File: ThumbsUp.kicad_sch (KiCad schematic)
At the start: 42 parts, among them J10 Raiser_Male, J13 Raiser_Female, J14 Raiser_Male, J19 Raiser_Female, J1L1 PJ-3200B, J1R1 PJ-3200B, J33 Raiser_Male, J34 Raiser_Female, J35 Raiser_Male, J38 Raiser_Female, J39 Raiser_Male, J40 Raiser_Female, J41 Raiser_Male, J47 Raiser_Female, J48 Raiser_Male, J9 Raiser_Female, U1 ProMicro

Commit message: K12: Modifying the layout, WIP.
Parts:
- added JP1: Handiness, Jumper:SolderJumper-2_P1.3mm_Open_RoundedPad1.0x1.5mm, symbol Jumper:SolderJumper_2_Open
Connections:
- net GND: now also JP1.1 (A)
- net at U1.7 (D4): now also JP1.2 (B)
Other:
- note added: "GP29 GP28 GP27 GP26 GP22 GP20 GP23 GP21"
- note added: "GP5 GP6 GP7 GP8 GP9"
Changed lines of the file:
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@@
 		)
 	)
+	(text "GP5\nGP6\nGP7\nGP8\nGP9"
+		(exclude_from_sim no)
+		(at 320.04 226.568 0)
+		(effects
+			(font
+				(size 1.27 1.27)
+			)
+		)
+	)
+	(text "GP29\nGP28\nGP27\nGP26\nGP22\nGP20\nGP23\nGP21"
+		(exclude_from_sim no)
+		(at 332.486 222.25 0)
+		(effects
+			(font
+				(size 1.27 1.27)
+			)
+		)
+	)
 	(junction
 		(at 303.53 308.61)
@@
 	(wire
 		(pts
+			(xy 295.91 218.44) (xy 297.18 218.44)
+		)
+		(stroke
+			(width 0)
+			(type default)
+		)
+	)
+	(wire
+		(pts
 			(xy 502.92 332.74) (xy 500.38 332.74)
 		)
@@
 	(wire
 		(pts
+			(xy 304.8 218.44) (xy 308.61 218.44)
+		)
+		(stroke
+			(width 0)
+			(type default)
+		)
+	)
+	(wire
+		(pts
 			(xy 438.15 199.39) (xy 438.15 207.01)
 		)
@@
 	(symbol
 		(lib_id "power:GND")
+		(at 295.91 218.44 0)
+		(unit 1)
+		(exclude_from_sim no)
+		(in_bom yes)
+		(on_board yes)
+		(dnp no)
+		(property "Reference" "#PWR08"
+			(at 295.91 224.79 0)
+			(effects
+				(font
+					(size 1.27 1.27)
+				)
+				(hide yes)
+			)
+		)
+		(property "Value" "GND"
+			(at 296.037 222.8342 0)
+			(effects
+				(font
+					(size 1.27 1.27)
+				)
+			)
+		)
+		(property "Footprint" ""
+			(at 295.91 218.44 0)
+			(effects
+				(font
+					(size 1.27 1.27)
+				)
+				(hide yes)
+			)
+		)
+		(property "Datasheet" ""
+			(at 295.91 218.44 0)
+			(effects
+				(font
+					(size 1.27 1.27)
+				)
+				(hide yes)
+			)
+		)
+		(property "Description" ""
+			(at 295.91 218.44 0)
+			(effects
+				(font
+					(size 1.27 1.27)
+				)
+			)
+		)
+		(pin "1"
+		)
+		(instances
+			(project "ThumbsUp"
+				(path "/467ed76c-995a-4514-a2e9-81ed0f98430e"
+					(reference "#PWR08")
+					(unit 1)
+				)
+			)
+		)
+	)
+	(symbol
+		(lib_id "power:GND")
 		(at 364.49 205.74 0)
 		(unit 1)
@@
 					(unit 1)
 				)
+			)
+		)
+	)
+	(symbol
+		(lib_id "Jumper:SolderJumper_2_Open")
+		(at 300.99 218.44 0)
+		(unit 1)
+		(exclude_from_sim no)
+		(in_bom no)
+		(on_board yes)
+		(dnp no)
+		(fields_autoplaced yes)
+		(property "Reference" "JP1"
+			(at 300.99 212.09 0)
+			(effects
+				(font
+					(size 1.27 1.27)
+				)
+			)
+		)
+		(property "Value" "Handiness"
+			(at 300.99 214.63 0)
+			(effects
+				(font
+					(size 1.27 1.27)
+				)
+			)
+		)
+		(property "Footprint" "Jumper:SolderJumper-2_P1.3mm_Open_RoundedPad1.0x1.5mm"
+			(at 300.99 218.44 0)
+			(effects
+				(font
+					(size 1.27 1.27)
+				)
+				(hide yes)
+			)
+		)
+		(property "Datasheet" "~"
+			(at 300.99 218.44 0)
+			(effects
+				(font
+					(size 1.27 1.27)
+				)
+				(hide yes)
+			)
+		)
+		(property "Description" "Solder Jumper, 2-pole, open"
+			(at 300.99 218.44 0)
+			(effects
+				(font
+					(size 1.27 1.27)
+				)
+				(hide yes)
+			)
+		)
+		(pin "1"
+		)
+		(pin "2"
+		)
+		(instances
+			(project ""
+				(path "/467ed76c-995a-4514-a2e9-81ed0f98430e"
+					(reference "JP1")
+					(unit 1)
+				)

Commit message: K12: Modifying the layout, WIP.
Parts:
- added H6: MountingHole_Pad, MountingHole:MountingHole_3.5mm_Pad, symbol Mechanical:MountingHole_Pad
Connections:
- net GNDB is gone; now on net GND: H3.1
- net GNDA: now also H6.1
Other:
- moved on the sheet: H1, H10, H15, H2

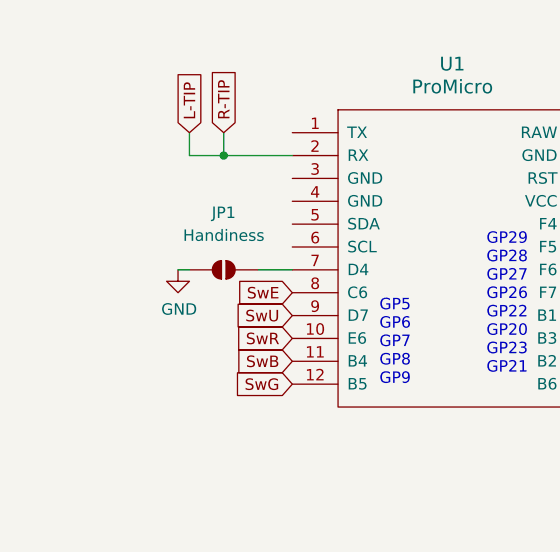
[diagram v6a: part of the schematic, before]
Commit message: K12: Added left-side handiness pull-up R, laid out all tracks. TODO: generate Gerbers.
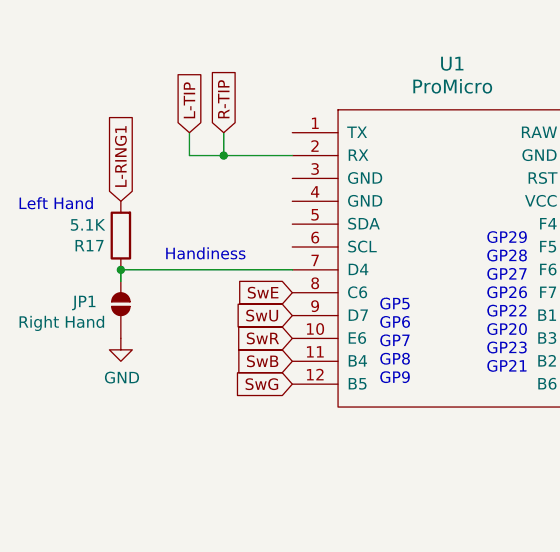
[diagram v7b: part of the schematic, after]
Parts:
- added R17: 5.1K, Resistor_SMD:R_0805_2012Metric, symbol Device:R
- JP1: value Handiness -> Right Hand
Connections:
- net +5V: now also R17.2
- net at JP1.2 (B), U1.7 (D4): now also R17.1
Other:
- note added: "Handiness"
- note added: "Left Hand"
- moved on the sheet: JP1
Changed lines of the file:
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@@
 		)
 	)
+	(text "Left Hand"
+		(exclude_from_sim no)
+		(at 278.13 212.09 0)
+		(effects
+			(font
+				(size 1.27 1.27)
+			)
+			(justify left bottom)
+		)
+	)
+	(text "Handiness"
+		(exclude_from_sim no)
+		(at 298.958 216.916 0)
+		(effects
+			(font
+				(size 1.27 1.27)
+			)
+		)
+	)
 	(junction
 		(at 303.53 308.61)
@@
 	)
 	(junction
+		(at 289.56 218.44)
+		(diameter 0)
+		(color 0 0 0 0)
+	)
+	(junction
 		(at 491.49 345.44)
 		(diameter 0)
@@
 	(wire
 		(pts
-			(xy 295.91 218.44) (xy 297.18 218.44)
+			(xy 502.92 332.74) (xy 500.38 332.74)
 		)
 		(stroke
@@
 	(wire
 		(pts
-			(xy 502.92 332.74) (xy 500.38 332.74)
+			(xy 414.02 345.44) (xy 416.56 345.44)
 		)
 		(stroke
@@
 	(wire
 		(pts
-			(xy 414.02 345.44) (xy 416.56 345.44)
+			(xy 317.5 299.72) (xy 328.93 299.72)
 		)
 		(stroke
@@
 	(wire
 		(pts
-			(xy 317.5 299.72) (xy 328.93 299.72)
+			(xy 289.56 219.71) (xy 289.56 218.44)
 		)
 		(stroke
@@
 	(wire
 		(pts
-			(xy 304.8 218.44) (xy 308.61 218.44)
-		)
-		(stroke
-			(width 0)
-			(type default)
-		)
-	)
-	(wire
-		(pts
 			(xy 438.15 199.39) (xy 438.15 207.01)
 		)
@@
 	(wire
 		(pts
+			(xy 289.56 218.44) (xy 308.61 218.44)
+		)
+		(stroke
+			(width 0)
+			(type default)
+		)
+	)
+	(wire
+		(pts
 			(xy 491.49 332.74) (xy 488.95 332.74)
 		)
@@
 		)
 	)
+	(global_label "L-RING1"
+		(shape input)
+		(at 289.56 210.82 90)
+		(effects
+			(font
+				(size 1.27 1.27)
+			)
+			(justify left)
+		)
+		(property "Intersheetrefs" "${INTERSHEET_REFS}"
+			(at 289.56 210.82 90)
+			(effects
+				(font
+					(size 1.27 1.27)
+				)
+				(hide yes)
+			)
+		)
+	)
 	(global_label "R-RING1"
 		(shape input)
@@
 	)
 	(symbol
+		(lib_id "Device:R")
+		(at 289.56 214.63 180)
+		(unit 1)
+		(exclude_from_sim no)
+		(in_bom yes)
+		(on_board yes)
+		(dnp no)
+		(property "Reference" "R17"
+			(at 287.782 215.7984 0)
+			(effects
+				(font
+					(size 1.27 1.27)
+				)
+				(justify left)
+			)
+		)
+		(property "Value" "5.1K"
+			(at 287.782 213.487 0)
+			(effects
+				(font
+					(size 1.27 1.27)
+				)
+				(justify left)
+			)
+		)
+		(property "Footprint" "Resistor_SMD:R_0805_2012Metric"
+			(at 291.338 214.63 90)
+			(effects
+				(font
+					(size 1.27 1.27)
+				)
+				(hide yes)
+			)
+		)
+		(property "Datasheet" "~"
+			(at 289.56 214.63 0)
+			(effects
+				(font
+					(size 1.27 1.27)
+				)
+				(hide yes)
+			)
+		)
+		(property "Description" ""
+			(at 289.56 214.63 0)
+			(effects
+				(font
+					(size 1.27 1.27)
+				)
+			)
+		)
+		(pin "2"
+		)
+		(pin "1"
+		)
+		(instances
+			(project "ThumbsUp"
+				(path "/467ed76c-995a-4514-a2e9-81ed0f98430e"
+					(reference "R17")
+					(unit 1)
+				)
+			)
+		)
+	)
+	(symbol
 		(lib_id "power:+5V")
 		(at 406.4 222.25 0)
@@
 	(symbol
 		(lib_id "power:GND")
-		(at 295.91 218.44 0)
+		(at 289.56 226.06 0)
 		(unit 1)
 		(exclude_from_sim no)
@@
 		(dnp no)
 		(property "Reference" "#PWR08"
-			(at 295.91 224.79 0)
+			(at 289.56 232.41 0)
 			(effects
 				(font
@@
 		)
 		(property "Value" "GND"
-			(at 296.037 222.8342 0)
+			(at 289.687 230.4542 0)
 			(effects
 				(font
@@
 		)
 		(property "Footprint" ""
-			(at 295.91 218.44 0)
+			(at 289.56 226.06 0)
 			(effects
 				(font
@@
 		)
 		(property "Datasheet" ""
-			(at 295.91 218.44 0)
+			(at 289.56 226.06 0)
 			(effects
 				(font
@@
 		)
 		(property "Description" ""
-			(at 295.91 218.44 0)
+			(at 289.56 226.06 0)
 			(effects
 				(font
@@
 	(symbol
 		(lib_id "Jumper:SolderJumper_2_Open")
-		(at 300.99 218.44 0)
+		(at 289.56 222.25 90)
 		(unit 1)
 		(exclude_from_sim no)
@@
 		(on_board yes)
 		(dnp no)
-		(fields_autoplaced yes)
 		(property "Reference" "JP1"
-			(at 300.99 212.09 0)
+			(at 284.226 221.996 90)
 			(effects
 				(font
 					(size 1.27 1.27)
 				)
+				(justify right)
 			)
 		)
-		(property "Value" "Handiness"
-			(at 300.99 214.63 0)
+		(property "Value" "Right Hand"
+			(at 278.13 224.282 90)
 			(effects
 				(font
 					(size 1.27 1.27)
 				)
+				(justify right)
 			)
 		)
 		(property "Footprint" "Jumper:SolderJumper-2_P1.3mm_Open_RoundedPad1.0x1.5mm"
-			(at 300.99 218.44 0)
+			(at 289.56 222.25 0)
 			(effects
 				(font
@@
 		)
 		(property "Datasheet" "~"
-			(at 300.99 218.44 0)
+			(at 289.56 222.25 0)
 			(effects
 				(font
@@
 		)
 		(property "Description" "Solder Jumper, 2-pole, open"
-			(at 300.99 218.44 0)
+			(at 289.56 222.25 0)
 			(effects
 				(font

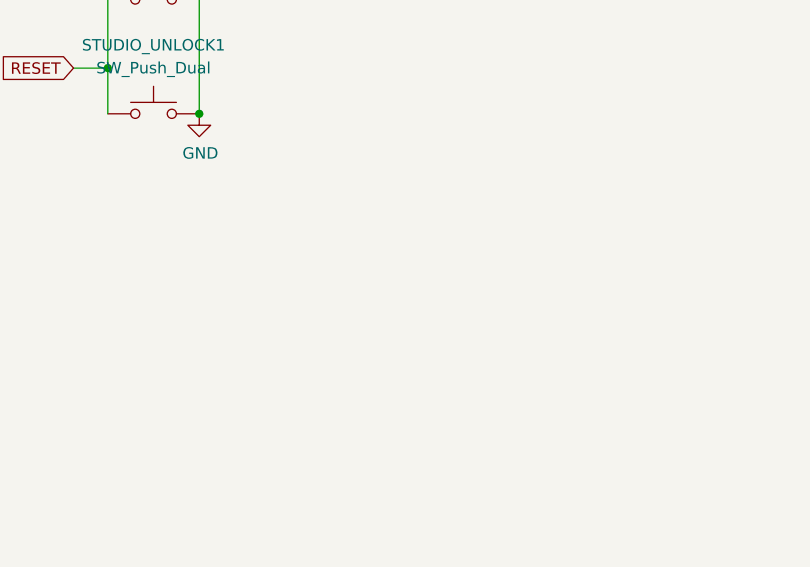
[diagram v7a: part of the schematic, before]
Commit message: K12: Doing modifications outlined for rev.3
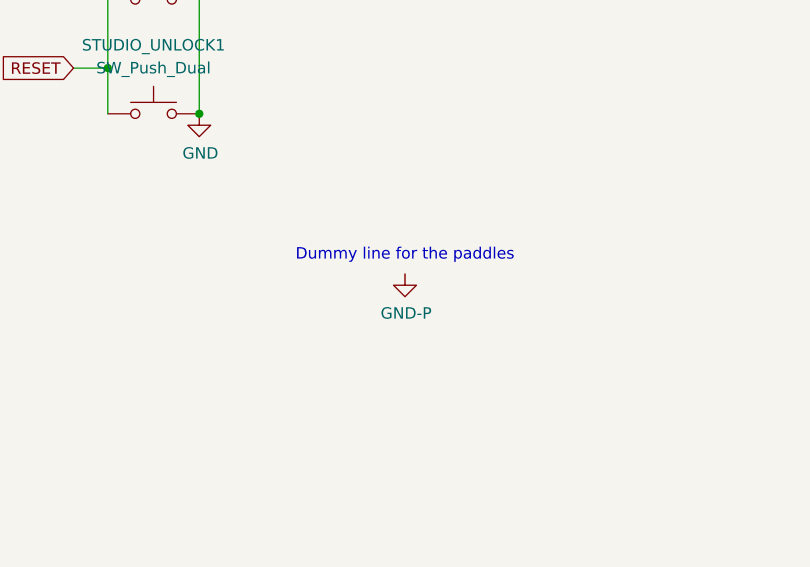
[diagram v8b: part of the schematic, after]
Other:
- note added: "Dummy line for the paddles"
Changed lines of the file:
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@@
 		)
 	)
+	(text "Dummy line for the paddles "
+		(exclude_from_sim no)
+		(at 471.17 227.838 0)
+		(effects
+			(font
+				(size 1.27 1.27)
+			)
+		)
+	)
 	(text "Handiness"
 		(exclude_from_sim no)
@@
 					(unit 1)
 				)
+			)
+		)
+	)
+	(symbol
+		(lib_id "power:GND")
+		(at 471.17 229.87 0)
+		(unit 1)
+		(exclude_from_sim no)
+		(in_bom yes)
+		(on_board yes)
+		(dnp no)
+		(property "Reference" "#PWR07"
+			(at 471.17 236.22 0)
+			(effects
+				(font
+					(size 1.27 1.27)
+				)
+				(hide yes)
+			)
+		)
+		(property "Value" "GND-P"
+			(at 471.297 234.2642 0)
+			(effects
+				(font
+					(size 1.27 1.27)
+				)
+			)
+		)
+		(property "Footprint" ""
+			(at 471.17 229.87 0)
+			(effects
+				(font
+					(size 1.27 1.27)
+				)
+				(hide yes)
+			)
+		)
+		(property "Datasheet" ""
+			(at 471.17 229.87 0)
+			(effects
+				(font
+					(size 1.27 1.27)
+				)
+				(hide yes)
+			)
+		)
+		(property "Description" ""
+			(at 471.17 229.87 0)
+			(effects
+				(font
+					(size 1.27 1.27)
+				)
+			)
+		)
+		(pin "1"
+		)
+		(instances
+			(project "ThumbsUp"
+				(path "/467ed76c-995a-4514-a2e9-81ed0f98430e"
+					(reference "#PWR07")
+					(unit 1)
+				)
